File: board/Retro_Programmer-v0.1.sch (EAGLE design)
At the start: 48 parts, among them IC1 74LVC125A, K1 61301511821, K2 61301511821, P1 POWERSUPPLY_DC21MMX, Q1 BC857CSMD, SW1 SPUSH, SW2 SPUSH, SW3 SPUSH, SW4 SLIDE_WAY4, T2 BC847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

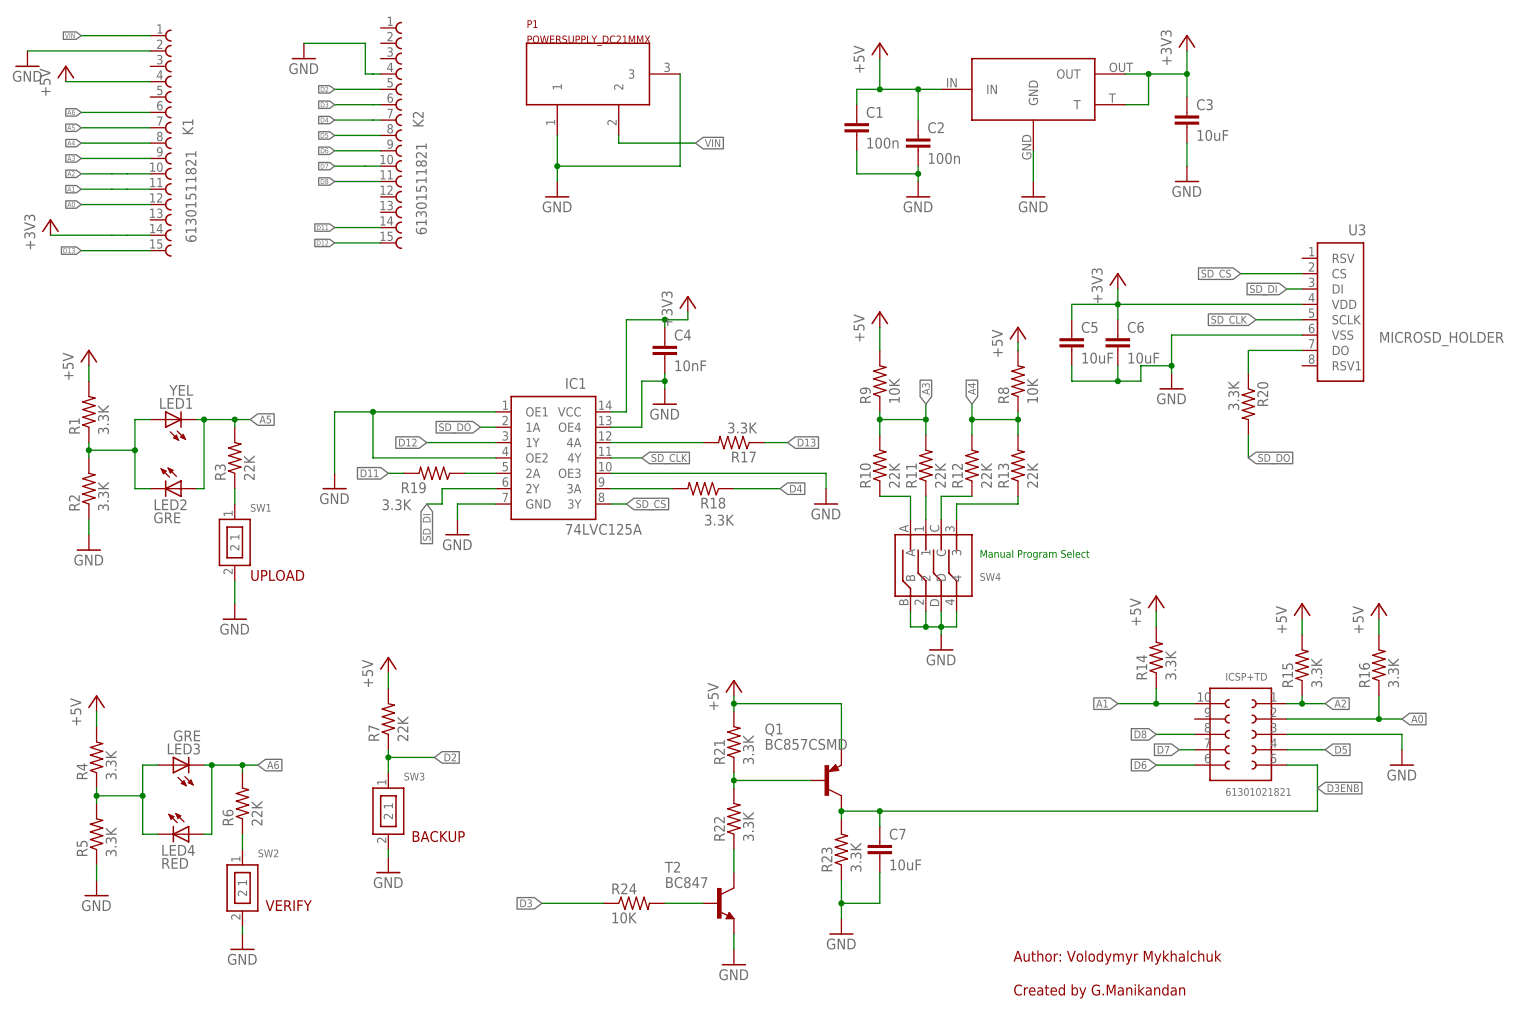
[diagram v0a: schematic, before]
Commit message: improved labelling on board
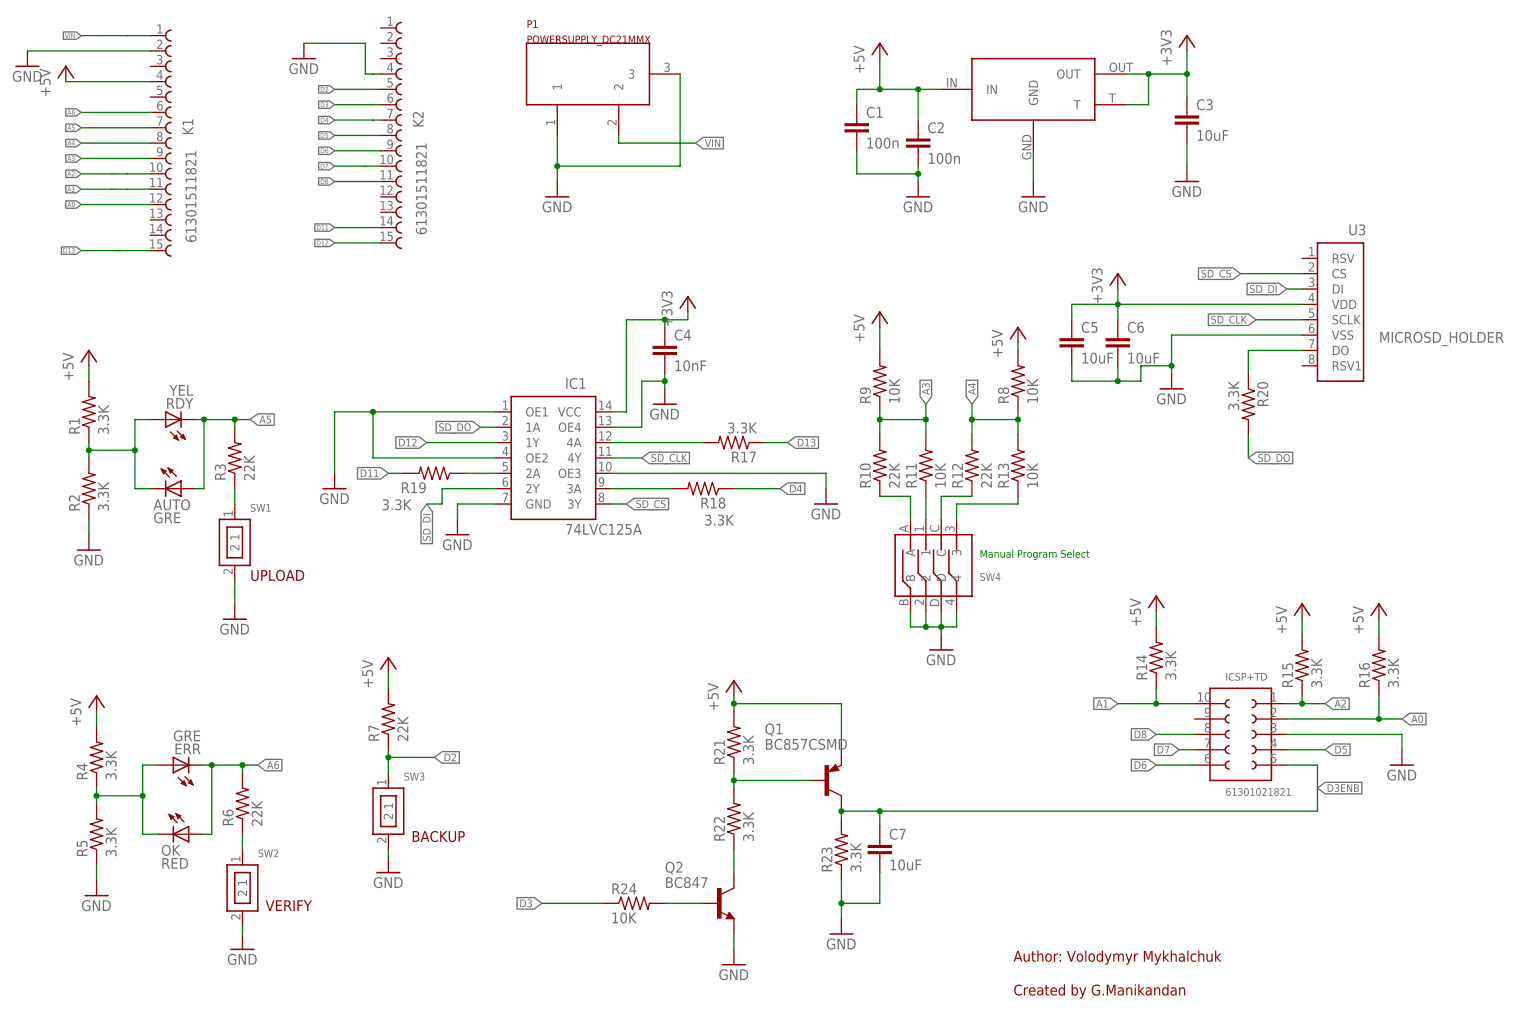
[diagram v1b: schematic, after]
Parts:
- R11, R13: value 22K -> 10K
- renumbered LED1 to RDY, LED2 to AUTO, LED3 to ERR, LED4 to OK, T2 to Q2
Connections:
- net +3V3: no longer K1.14
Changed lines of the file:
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@@
 <part name="GND1" library="supply1" deviceset="GND" device=""/>
 <part name="P+1" library="supply1" deviceset="+5V" device=""/>
-<part name="+3V1" library="supply1" deviceset="+3V3" device=""/>
 <part name="GND2" library="supply1" deviceset="GND" device=""/>
 <part name="R1" library="rcl" deviceset="R-US_" device="R1206" value="3.3K"/>
@@
 <part name="P+2" library="supply1" deviceset="+5V" device=""/>
 <part name="GND3" library="supply1" deviceset="GND" device=""/>
-<part name="LED1" library="led" deviceset="LED" device="CHIPLED_1206" value="YEL"/>
-<part name="LED2" library="led" deviceset="LED" device="CHIPLED_1206" value="GRE"/>
+<part name="RDY" library="led" deviceset="LED" device="CHIPLED_1206" value="YEL"/>
+<part name="AUTO" library="led" deviceset="LED" device="CHIPLED_1206" value="GRE"/>
 <part name="SW1" library="Ard" deviceset="SPUSH" device=""/>
 <part name="R3" library="rcl" deviceset="R-US_" device="R1206" value="22K"/>
@@
 <part name="P+3" library="supply1" deviceset="+5V" device=""/>
 <part name="GND5" library="supply1" deviceset="GND" device=""/>
-<part name="LED3" library="led" deviceset="LED" device="CHIPLED_1206" value="GRE"/>
-<part name="LED4" library="led" deviceset="LED" device="CHIPLED_1206" value="RED"/>
+<part name="ERR" library="led" deviceset="LED" device="CHIPLED_1206" value="GRE"/>
+<part name="OK" library="led" deviceset="LED" device="CHIPLED_1206" value="RED"/>
 <part name="SW2" library="Ard" deviceset="SPUSH" device=""/>
 <part name="R6" library="rcl" deviceset="R-US_" device="R1206" value="22K"/>
@@
 <part name="+3V2" library="supply1" deviceset="+3V3" device=""/>
 <part name="R10" library="rcl" deviceset="R-US_" device="R1206" value="22K"/>
-<part name="R11" library="rcl" deviceset="R-US_" device="R1206" value="22K"/>
+<part name="R11" library="rcl" deviceset="R-US_" device="R1206" value="10K"/>
 <part name="R12" library="rcl" deviceset="R-US_" device="R1206" value="22K"/>
-<part name="R13" library="rcl" deviceset="R-US_" device="R1206" value="22K"/>
+<part name="R13" library="rcl" deviceset="R-US_" device="R1206" value="10K"/>
 <part name="R9" library="rcl" deviceset="R-US_" device="R1206" value="10K"/>
 <part name="P+5" library="supply1" deviceset="+5V" device=""/>
@@
 <part name="R22" library="rcl" deviceset="R-US_" device="R1206" value="3.3K"/>
 <part name="P+11" library="supply1" deviceset="+5V" device=""/>
-<part name="T2" library="transistor" deviceset="BC847" device=""/>
+<part name="Q2" library="transistor" deviceset="BC847" device=""/>
 <part name="GND18" library="supply1" deviceset="GND" device=""/>
 <part name="Q1" library="transistor-pnp" deviceset="BC857*" device="SMD" technology="C"/>
@@
 <instance part="GND1" gate="1" x="5.08" y="165.1"/>
 <instance part="P+1" gate="1" x="11.43" y="165.1"/>
-<instance part="+3V1" gate="G$1" x="8.89" y="139.7"/>
 <instance part="GND2" gate="1" x="50.8" y="166.37"/>
 <instance part="R1" gate="G$1" x="15.24" y="107.95" rot="R90"/>
@@
 <instance part="P+2" gate="1" x="15.24" y="118.11"/>
 <instance part="GND3" gate="1" x="15.24" y="85.09"/>
-<instance part="LED1" gate="G$1" x="27.94" y="106.68" rot="R90"/>
-<instance part="LED2" gate="G$1" x="30.48" y="95.25" rot="R270"/>
+<instance part="RDY" gate="G$1" x="27.94" y="106.68" rot="R90"/>
+<instance part="AUTO" gate="G$1" x="30.48" y="95.25" rot="R270"/>
 <instance part="SW1" gate="G$1" x="39.37" y="86.36"/>
 <instance part="R3" gate="G$1" x="39.37" y="100.33" rot="R90"/>
@@
 <instance part="P+3" gate="1" x="16.51" y="60.96"/>
 <instance part="GND5" gate="1" x="16.51" y="27.94"/>
-<instance part="LED3" gate="G$1" x="29.21" y="49.53" rot="R90"/>
-<instance part="LED4" gate="G$1" x="31.75" y="38.1" rot="R270"/>
+<instance part="ERR" gate="G$1" x="29.21" y="49.53" rot="R90"/>
+<instance part="OK" gate="G$1" x="31.75" y="38.1" rot="R270"/>
 <instance part="SW2" gate="G$1" x="40.64" y="29.21"/>
 <instance part="R6" gate="G$1" x="40.64" y="43.18" rot="R90"/>
@@
 <instance part="R22" gate="G$1" x="121.92" y="40.64" rot="R90"/>
 <instance part="P+11" gate="1" x="121.92" y="63.5"/>
-<instance part="T2" gate="G$1" x="119.38" y="26.67" smashed="yes">
+<instance part="Q2" gate="G$1" x="119.38" y="26.67" smashed="yes">
 <attribute name="NAME" x="110.49" y="31.75" size="1.778" layer="95"/>
 <attribute name="VALUE" x="110.49" y="29.21" size="1.778" layer="96"/>
@@
 </segment>
 <segment>
-<pinref part="LED3" gate="G$1" pin="C"/>
+<pinref part="ERR" gate="G$1" pin="C"/>
 <wire x1="34.29" y1="49.53" x2="35.56" y2="49.53" width="0.1524" layer="91"/>
 <wire x1="35.56" y1="49.53" x2="35.56" y2="38.1" width="0.1524" layer="91"/>
@@
 <junction x="40.64" y="49.53"/>
 <label x="43.18" y="49.53" size="1.27" layer="95" xref="yes"/>
-<pinref part="LED4" gate="G$1" pin="A"/>
+<pinref part="OK" gate="G$1" pin="A"/>
 </segment>
 </net>
@@
 </segment>
 <segment>
-<pinref part="LED1" gate="G$1" pin="C"/>
+<pinref part="RDY" gate="G$1" pin="C"/>
 <wire x1="33.02" y1="106.68" x2="34.29" y2="106.68" width="0.1524" layer="91"/>
 <wire x1="34.29" y1="106.68" x2="34.29" y2="95.25" width="0.1524" layer="91"/>
@@
 <junction x="39.37" y="106.68"/>
 <label x="41.91" y="106.68" size="1.27" layer="95" xref="yes"/>
-<pinref part="LED2" gate="G$1" pin="A"/>
+<pinref part="AUTO" gate="G$1" pin="A"/>
 </segment>
 </net>
@@
 </segment>
 <segment>
-<pinref part="T2" gate="G$1" pin="E"/>
+<pinref part="Q2" gate="G$1" pin="E"/>
 <wire x1="121.92" y1="21.59" x2="121.92" y2="19.05" width="0.1524" layer="91"/>
 <pinref part="GND18" gate="1" pin="GND"/>
@@
 <net name="+3V3" class="0">
 <segment>
-<pinref part="+3V1" gate="G$1" pin="+3V3"/>
-<wire x1="21.59" y1="137.16" x2="19.05" y2="137.16" width="0.1524" layer="91"/>
-<wire x1="19.05" y1="137.16" x2="8.89" y2="137.16" width="0.1524" layer="91"/>
-<pinref part="K1" gate="G$1" pin="14"/>
-<wire x1="25.4" y1="137.16" x2="21.59" y2="137.16" width="0.1524" layer="91"/>
-</segment>
-<segment>
 <pinref part="C3" gate="G$1" pin="1"/>
 <wire x1="196.85" y1="163.83" x2="196.85" y2="160.02" width="0.1524" layer="91"/>
@@
 <wire x1="15.24" y1="101.6" x2="22.86" y2="101.6" width="0.1524" layer="91"/>
 <wire x1="22.86" y1="101.6" x2="22.86" y2="106.68" width="0.1524" layer="91"/>
-<pinref part="LED1" gate="G$1" pin="A"/>
+<pinref part="RDY" gate="G$1" pin="A"/>
 <wire x1="22.86" y1="106.68" x2="25.4" y2="106.68" width="0.1524" layer="91"/>
 <wire x1="22.86" y1="101.6" x2="22.86" y2="95.25" width="0.1524" layer="91"/>
-<pinref part="LED2" gate="G$1" pin="C"/>
+<pinref part="AUTO" gate="G$1" pin="C"/>
 <wire x1="22.86" y1="95.25" x2="25.4" y2="95.25" width="0.1524" layer="91"/>
 <junction x="15.24" y="101.6"/>
@@
 <wire x1="16.51" y1="44.45" x2="24.13" y2="44.45" width="0.1524" layer="91"/>
 <wire x1="24.13" y1="44.45" x2="24.13" y2="49.53" width="0.1524" layer="91"/>
-<pinref part="LED3" gate="G$1" pin="A"/>
+<pinref part="ERR" gate="G$1" pin="A"/>
 <wire x1="24.13" y1="49.53" x2="26.67" y2="49.53" width="0.1524" layer="91"/>
 <wire x1="24.13" y1="44.45" x2="24.13" y2="38.1" width="0.1524" layer="91"/>
-<pinref part="LED4" gate="G$1" pin="C"/>
+<pinref part="OK" gate="G$1" pin="C"/>
 <wire x1="24.13" y1="38.1" x2="26.67" y2="38.1" width="0.1524" layer="91"/>
 <junction x="16.51" y="44.45"/>
@@
 <segment>
 <pinref part="R22" gate="G$1" pin="1"/>
-<pinref part="T2" gate="G$1" pin="C"/>
+<pinref part="Q2" gate="G$1" pin="C"/>
 <wire x1="121.92" y1="35.56" x2="121.92" y2="31.75" width="0.1524" layer="91"/>
 </segment>
@@
 <net name="N$15" class="0">
 <segment>
-<pinref part="T2" gate="G$1" pin="B"/>
+<pinref part="Q2" gate="G$1" pin="B"/>
 <wire x1="116.84" y1="26.67" x2="110.49" y2="26.67" width="0.1524" layer="91"/>
 <pinref part="R24" gate="G$1" pin="2"/>

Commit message: More bla bla bla
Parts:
- C2: value 100n -> 100nF
- C5: value 10uF -> 100nF
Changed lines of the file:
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@@
 <part name="ICSP+TD" library="Wuerth_Elektronik_Board_to_Board" deviceset="61301021821" device=""/>
 <part name="GND7" library="supply1" deviceset="GND" device=""/>
-<part name="C2" library="rcl" deviceset="C-EU" device="C1206" value="100n"/>
+<part name="C2" library="rcl" deviceset="C-EU" device="C1206" value="100nF"/>
 <part name="C3" library="rcl" deviceset="C-EU" device="C1206" value="10uF"/>
 <part name="GND8" library="supply1" deviceset="GND" device=""/>
@@
 <part name="GND14" library="supply1" deviceset="GND" device=""/>
 <part name="+3V4" library="supply1" deviceset="+3V3" device=""/>
-<part name="C5" library="rcl" deviceset="C-EU" device="C1206" value="10uF"/>
+<part name="C5" library="rcl" deviceset="C-EU" device="C1206" value="100nF"/>
 <part name="C6" library="rcl" deviceset="C-EU" device="C1206" value="10uF"/>
 <part name="GND15" library="supply1" deviceset="GND" device=""/>
